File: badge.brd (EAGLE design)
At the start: 90.7 x 92.4 mm, 178 parts, among them CN4 MicroUSB, IC3 MEGA8-AI, Q1 BSS138, Q2 BSS138, T1 MMUN2133LT1G, U1 TPS61090RSAR, U2 MCP73871, U3 LIS3DHTR, U4 MIC5225-3.3, Y1 16.00MHz

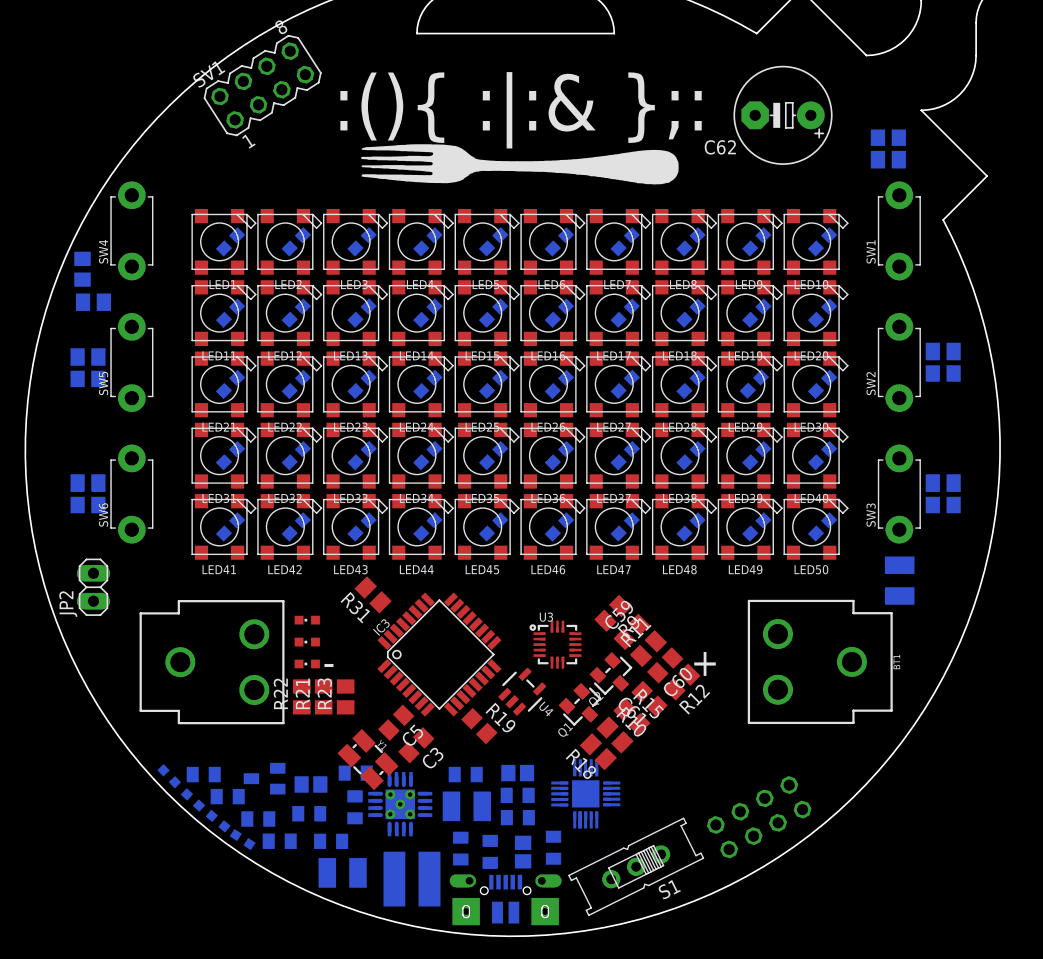
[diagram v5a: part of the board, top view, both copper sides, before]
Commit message: -wired all the pixels -cleaned up the schematic
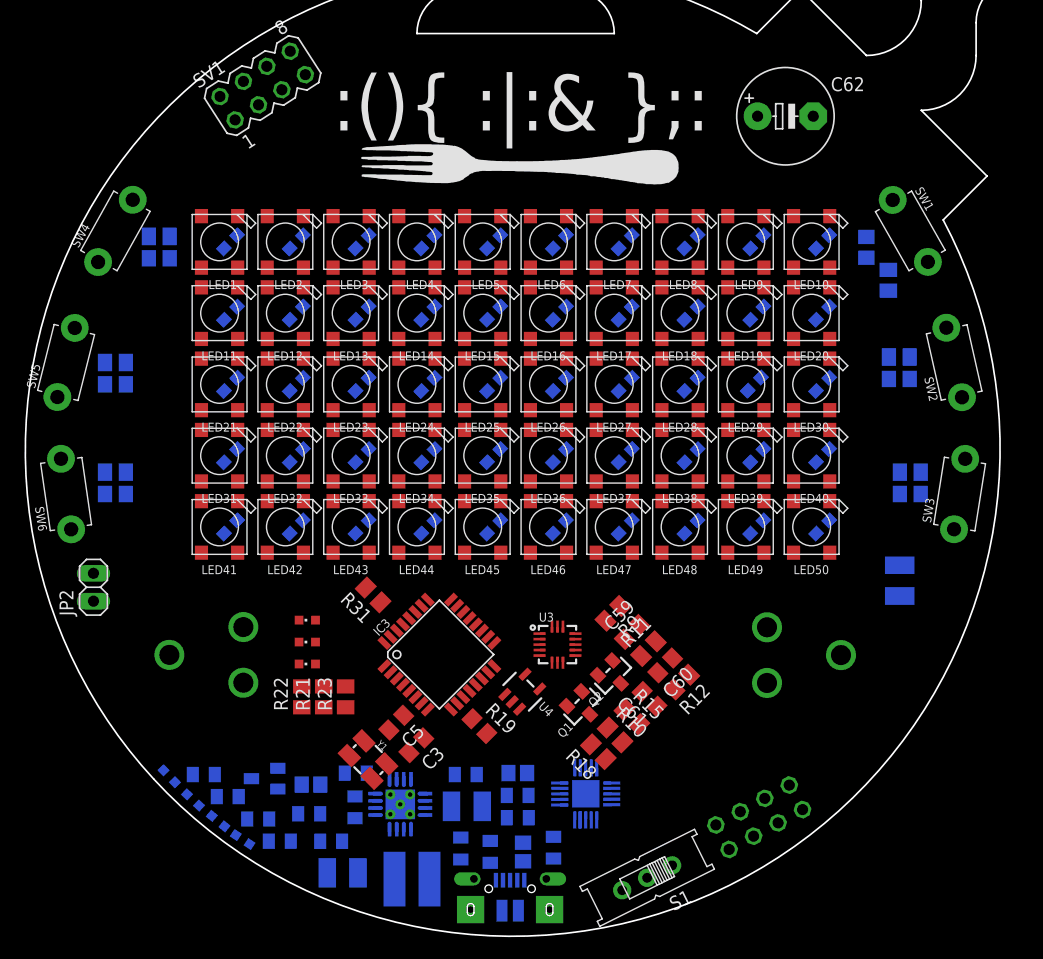
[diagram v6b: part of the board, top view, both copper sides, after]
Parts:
- moved R24 11.0 mm to (80.0, 60.5), turned to 270 degrees
- moved C63 10.2 mm to (78.0, 63.5), turned to 270 degrees
- moved R27 8.49 mm to (13.5, 64.5)
- moved C66 7.07 mm to (13.5, 62.5), turned to 0 degrees
- moved SW5 6.00 mm to (5.00, 53.0), turned to 75.9 degrees
- moved SW6 6.00 mm to (5.00, 41.0), turned to 98.2 degrees
- moved SW3 5.50 mm to (86.5, 41.0), turned to 81 degrees
- moved SW2 5.00 mm to (86.0, 53.0), turned to 102.7 degrees
- moved C64 4.03 mm to (81.0, 51.5)
- moved R25 4.03 mm to (81.0, 53.5)
- moved C65 3.16 mm to (82.0, 41.0)
- moved R26 3.16 mm to (82.0, 43.0)
- moved C68 2.69 mm to (9.50, 41.0)
- moved R29 2.69 mm to (9.50, 43.0)
- moved C67 2.55 mm to (9.50, 51.0)
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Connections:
- removed net N$18: C9.2, LED1.3-GND
- removed net VDD: LED10.1-VDD, LED11.1-VDD, LED12.1-VDD, LED13.1-VDD, LED14.1-VDD, LED15.1-VDD, LED16.1-VDD, LED17.1-VDD, LED18.1-VDD, LED19.1-VDD, LED2.1-VDD, LED20.1-VDD, LED21.1-VDD, LED22.1-VDD, LED23.1-VDD, LED24.1-VDD, LED25.1-VDD, LED26.1-VDD, LED27.1-VDD, LED28.1-VDD, LED29.1-VDD, LED3.1-VDD, LED30.1-VDD, LED31.1-VDD, LED32.1-VDD, LED33.1-VDD, LED34.1-VDD, LED35.1-VDD, LED36.1-VDD, LED37.1-VDD, LED38.1-VDD, LED39.1-VDD, LED4.1-VDD, LED40.1-VDD, LED41.1-VDD, LED42.1-VDD, LED43.1-VDD, LED44.1-VDD, LED45.1-VDD, LED46.1-VDD, LED47.1-VDD, LED48.1-VDD, LED49.1-VDD, LED5.1-VDD, LED50.1-VDD, LED6.1-VDD, LED7.1-VDD, LED8.1-VDD, LED9.1-VDD
- new net N$24: LED1.2-DOUT, LED2.4-DIN
- new net N$25: LED3.2-DOUT, LED4.4-DIN
- new net N$26: LED4.2-DOUT, LED5.4-DIN
- new net N$27: LED5.2-DOUT, LED6.4-DIN
- new net N$37: LED6.2-DOUT, LED7.4-DIN
- new net N$38: LED7.2-DOUT, LED8.4-DIN
- new net N$39: LED8.2-DOUT, LED9.4-DIN
- new net N$40: LED10.4-DIN, LED9.2-DOUT
- new net N$41: LED10.2-DOUT, LED11.4-DIN
- new net N$42: LED11.2-DOUT, LED12.4-DIN
- new net N$43: LED12.2-DOUT, LED13.4-DIN
- new net N$44: LED13.2-DOUT, LED14.4-DIN
- new net N$45: LED14.2-DOUT, LED15.4-DIN
- new net N$46: LED15.2-DOUT, LED16.4-DIN
- new net N$47: LED16.2-DOUT, LED17.4-DIN
- new net N$48: LED17.2-DOUT, LED18.4-DIN
- new net N$49: LED18.2-DOUT, LED19.4-DIN
- new net N$50: LED19.2-DOUT, LED20.4-DIN
- new net N$51: LED20.2-DOUT, LED21.4-DIN
- new net N$52: LED21.2-DOUT, LED22.4-DIN
- new net N$53: LED22.2-DOUT, LED23.4-DIN
- new net N$54: LED23.2-DOUT, LED24.4-DIN
- new net N$55: LED24.2-DOUT, LED25.4-DIN
- new net N$56: LED25.2-DOUT, LED26.4-DIN
- new net N$57: LED26.2-DOUT, LED27.4-DIN
- new net N$58: LED27.2-DOUT, LED28.4-DIN
- new net N$59: LED28.2-DOUT, LED29.4-DIN
- new net N$60: LED29.2-DOUT, LED30.4-DIN
- new net N$61: LED30.2-DOUT, LED31.4-DIN
- new net N$62: LED31.2-DOUT, LED32.4-DIN
- new net N$63: LED32.2-DOUT, LED33.4-DIN
- new net N$64: LED33.2-DOUT, LED34.4-DIN
- new net N$65: LED34.2-DOUT, LED35.4-DIN
- new net N$66: LED35.2-DOUT, LED36.4-DIN
- new net N$67: LED36.2-DOUT, LED37.4-DIN
- new net N$68: LED37.2-DOUT, LED38.4-DIN
- new net N$69: LED38.2-DOUT, LED39.4-DIN
- new net N$70: LED39.2-DOUT, LED40.4-DIN
- new net N$71: LED40.2-DOUT, LED41.4-DIN
- new net N$72: LED41.2-DOUT, LED42.4-DIN
- new net N$73: LED42.2-DOUT, LED43.4-DIN
- new net N$74: LED43.2-DOUT, LED44.4-DIN
- new net N$75: LED44.2-DOUT, LED45.4-DIN
- new net N$76: LED45.2-DOUT, LED46.4-DIN
- new net N$77: LED46.2-DOUT, LED47.4-DIN
- new net N$78: LED47.2-DOUT, LED48.4-DIN
- new net N$79: LED48.2-DOUT, LED49.4-DIN
- new net N$80: LED49.2-DOUT, LED50.4-DIN
- new net PIXEL_DATA: LED1.4-DIN, R19.2
- net +5V: now also C10.1, C11.1, C12.1, C13.1, C14.1, C15.1, C16.1, C17.1, C18.1, C19.1, C20.1, C21.1, C22.1, C23.1, C24.1, C25.1, C26.1, C27.1, C28.1, C29.1, C30.1, C31.1, C32.1, C33.1, C34.1, C35.1, C36.1, C37.1, C38.1, C39.1, C40.1, C41.1, C42.1, C43.1, C44.1, C45.1, C46.1, C47.1, C48.1, C49.1, C50.1, C51.1, C52.1, C53.1, C54.1, C55.1, C56.1, C57.1, C58.1, C9.1, LED1.1-VDD, LED10.1-VDD, LED11.1-VDD, LED12.1-VDD, LED13.1-VDD, LED14.1-VDD, LED15.1-VDD, LED16.1-VDD, LED17.1-VDD, LED18.1-VDD, LED19.1-VDD, LED2.1-VDD, LED20.1-VDD, LED21.1-VDD, LED22.1-VDD, LED23.1-VDD, LED24.1-VDD, LED25.1-VDD, LED26.1-VDD, LED27.1-VDD, LED28.1-VDD, LED29.1-VDD, LED3.1-VDD, LED30.1-VDD, LED31.1-VDD, LED32.1-VDD, LED33.1-VDD, LED34.1-VDD, LED35.1-VDD, LED36.1-VDD, LED37.1-VDD, LED38.1-VDD, LED39.1-VDD, LED4.1-VDD, LED40.1-VDD, LED41.1-VDD, LED42.1-VDD, LED43.1-VDD, LED44.1-VDD, LED45.1-VDD, LED46.1-VDD, LED47.1-VDD, LED48.1-VDD, LED49.1-VDD, LED5.1-VDD, LED50.1-VDD, LED6.1-VDD, LED7.1-VDD, LED8.1-VDD, LED9.1-VDD
- net GND: now also C10.2, C11.2, C12.2, C13.2, C14.2, C15.2, C16.2, C17.2, C18.2, C19.2, C20.2, C21.2, C22.2, C23.2, C24.2, C25.2, C26.2, C27.2, C28.2, C29.2, C30.2, C31.2, C32.2, C33.2, C34.2, C35.2, C36.2, C37.2, C38.2, C39.2, C40.2, C41.2, C42.2, C43.2, C44.2, C45.2, C46.2, C47.2, C48.2, C49.2, C50.2, C51.2, C52.2, C53.2, C54.2, C55.2, C56.2, C57.2, C58.2, C63.2, C64.2, C65.2, C66.2, C67.2, C68.2, C9.2, LED1.3-GND
- net N$17: now also LED2.2-DOUT, LED3.4-DIN; no longer C9.1, LED1.1-VDD

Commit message: haha forget to save fuck me
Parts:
- removed SV1: (no value), con-lstb:MA04-2
- added JP3: TCVR_HEADER, pinhead:2X04
- JP2: value (none) -> PIEZO_HEADER
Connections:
- removed net ADC1: U3.16
- removed net ADC2: U3.15
- removed net ADC3: U3.13
- removed net INT1: U3.11
- removed net STAT4: STAT2.A
- net 3.3V: now also JP3.7; no longer SV1.7
- net CE\: now also JP3.6; no longer SV1.6
- net CSN: now also JP3.5; no longer SV1.5
- net GND: now also JP3.8; no longer SV1.8
- net MISO: now also JP3.2; no longer SV1.2
- net MOSI: now also JP3.3; no longer SV1.3
- net SCK: now also JP3.4; no longer SV1.4
- net STAT2: now also STAT2.A
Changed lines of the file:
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@@
 <wire x1="55" y1="83" x2="51" y2="87" width="0.1524" layer="20" curve="90"/>
 <wire x1="51" y1="87" x2="41" y2="87" width="0.1524" layer="20"/>
+<dimension x1="0" y1="0" x2="100" y2="0" x3="50" y3="-6" textsize="1.778" layer="51"/>
+<dimension x1="100" y1="0" x2="100" y2="100" x3="105.5" y3="50" textsize="1.778" layer="51"/>
 </plain>
 <attributes>
@@
 <element name="U4" library="microbuilder" package="SOT23-5" value="MIC5225-3.3" x="46.6109125" y="22.974875" rot="R315"/>
 <element name="C61" library="resistor" library_urn="urn:adsk.eagle:library:348" package="C0805" package3d_urn="urn:adsk.eagle:package:26137/1" value="10µF" x="58.215828125" y="22.316" rot="R135"/>
-<element name="SV1" library="con-lstb" library_urn="urn:adsk.eagle:library:162" package="MA04-2" package3d_urn="urn:adsk.eagle:package:8368/1" value="" x="22.93" y="78.256" rot="R32.8">
-<attribute name="MF" value="" x="22.93" y="78.256" size="1.778" layer="27" rot="R32.8" display="off"/>
-<attribute name="MPN" value="" x="22.93" y="78.256" size="1.778" layer="27" rot="R32.8" display="off"/>
-<attribute name="OC_FARNELL" value="unknown" x="22.93" y="78.256" size="1.778" layer="27" rot="R32.8" display="off"/>
-<attribute name="OC_NEWARK" value="unknown" x="22.93" y="78.256" size="1.778" layer="27" rot="R32.8" display="off"/>
-</element>
 <element name="SW1" library="adafruit" library_urn="urn:adsk.eagle:library:420" package="TACT_PANA-EVQ" value="" x="82" y="65" rot="R299.6"/>
 <element name="SW2" library="adafruit" library_urn="urn:adsk.eagle:library:420" package="TACT_PANA-EVQ" value="" x="86" y="53" rot="R102.7"/>
@@
 <element name="R19" library="resistor" library_urn="urn:adsk.eagle:library:348" package="R0805" package3d_urn="urn:adsk.eagle:package:26059/1" value="470" x="42.697571875" y="19.832134375" rot="R315"/>
 <element name="C62" library="resistor" library_urn="urn:adsk.eagle:library:348" package="E5-8,5" package3d_urn="urn:adsk.eagle:package:25860/1" value="1F" x="70.61" y="75.46"/>
-<element name="JP2" library="pinhead" library_urn="urn:adsk.eagle:library:325" package="1X02" package3d_urn="urn:adsk.eagle:package:22435/2" value="" x="7.5" y="32.5" rot="R90"/>
+<element name="JP2" library="pinhead" library_urn="urn:adsk.eagle:library:325" package="1X02" package3d_urn="urn:adsk.eagle:package:22435/2" value="PIEZO_HEADER" x="7.5" y="32.5" rot="R90"/>
 <element name="S1" library="adafruit" library_urn="urn:adsk.eagle:library:420" package="EG1218" value="" x="58" y="6" rot="R206.5"/>
 <element name="STAT1" library="piboy_new" package="ADAFRUIT_CHIPLED_0603" value="GREEN" x="27" y="29.5" rot="R90"/>
@@
 <element name="R29" library="resistor" library_urn="urn:adsk.eagle:library:348" package="M0805" package3d_urn="urn:adsk.eagle:package:26079/1" value="1k" x="9.5" y="43" rot="MR180"/>
 <element name="C68" library="resistor" library_urn="urn:adsk.eagle:library:348" package="C0805" package3d_urn="urn:adsk.eagle:package:26137/1" value="100nF" x="9.5" y="41" rot="MR180"/>
+<element name="JP3" library="pinhead" library_urn="urn:adsk.eagle:library:325" package="2X04" package3d_urn="urn:adsk.eagle:package:22461/2" value="TCVR_HEADER" x="21" y="77" rot="R39.3"/>
 </elements>
 <signals>
@@
 <contactref element="R18" pad="1"/>
 <contactref element="C61" pad="2"/>
-<contactref element="SV1" pad="8"/>
 <contactref element="C62" pad="-"/>
 <contactref element="JP2" pad="2"/>
@@
 <contactref element="C67" pad="2"/>
 <contactref element="C68" pad="2"/>
+<contactref element="JP3" pad="8"/>
 <wire x1="74.65" y1="66.35" x2="73.15" y2="75.46" width="0" layer="19" extent="1-1"/>
 <wire x1="74.60104375" y1="64.601040625" x2="74.65" y2="66.35" width="0" layer="19" extent="1-16"/>
@@
 <wire x1="8.55" y1="51" x2="10.45" y2="41" width="0" layer="19" extent="16-16"/>
 <wire x1="4.20825" y1="49.847915625" x2="8.55" y2="51" width="0" layer="19" extent="16-16"/>
-<wire x1="25.4445875" y1="81.387425" x2="26.65" y2="66.35" width="0" layer="19" extent="1-1"/>
+<wire x1="23.143934375" y1="80.39595625" x2="20.65" y2="66.35" width="0" layer="19" extent="1-1"/>
 <wire x1="69.940290625" y1="11.01049375" x2="55.726865625" y2="4.86665625" width="0" layer="19" extent="1-1"/>
 </signal>
@@
 <contactref element="JP1" pad="1"/>
 <contactref element="IC3" pad="16"/>
-<contactref element="SV1" pad="2"/>
-<wire x1="44.06610625" y1="25.30510625" x2="19.03946875" y2="77.259609375" width="0" layer="19" extent="1-1"/>
+<contactref element="JP3" pad="2"/>
+<wire x1="44.06610625" y1="25.30510625" x2="17.247275" y2="75.56959375" width="0" layer="19" extent="1-1"/>
 <wire x1="64.263915625" y1="10.818721875" x2="44.06610625" y2="25.30510625" width="0" layer="19" extent="1-1"/>
 </signal>
@@
 <contactref element="JP1" pad="3"/>
 <contactref element="IC3" pad="17"/>
-<contactref element="SV1" pad="4"/>
-<wire x1="44.06610625" y1="27.415959375" x2="21.174509375" y2="78.63555" width="0" layer="19" extent="1-1"/>
+<contactref element="JP3" pad="4"/>
+<wire x1="44.06610625" y1="27.415959375" x2="19.212828125" y2="77.17838125" width="0" layer="19" extent="1-1"/>
 <wire x1="66.4961125" y1="12.030703125" x2="44.06610625" y2="27.415959375" width="0" layer="19" extent="1-1"/>
 </signal>
@@
 <contactref element="JP1" pad="4"/>
 <contactref element="IC3" pad="15"/>
-<contactref element="SV1" pad="3"/>
-<wire x1="43.50041875" y1="24.73941875" x2="22.550446875" y2="76.500509375" width="0" layer="19" extent="1-1"/>
+<contactref element="JP3" pad="3"/>
+<wire x1="43.50041875" y1="24.73941875" x2="20.821615625" y2="75.212828125" width="0" layer="19" extent="1-1"/>
 <wire x1="67.708096875" y1="9.798509375" x2="43.50041875" y2="24.73941875" width="0" layer="19" extent="1-1"/>
 </signal>
@@
 <contactref element="U4" pad="5"/>
 <contactref element="R9" pad="1"/>
-<contactref element="SV1" pad="7"/>
-<wire x1="48.47" y1="28.27" x2="26.820528125" y2="79.2523875" width="0" layer="19" extent="1-1"/>
+<contactref element="JP3" pad="7"/>
+<wire x1="48.47" y1="28.27" x2="24.752721875" y2="78.430403125" width="0" layer="19" extent="1-1"/>
 <wire x1="50.32" y1="28.62" x2="48.47" y2="28.27" width="0" layer="19" extent="1-1"/>
 <wire x1="46.85846875" y1="24.565934375" x2="48.47" y2="28.27" width="0" layer="19" extent="1-1"/>
@@
 <wire x1="36.298396875" y1="29.678703125" x2="55.59619375" y2="23.73223125" width="0" layer="19" extent="1-1"/>
 </signal>
-<signal name="INT1">
-<contactref element="U3" pad="11"/>
-</signal>
 <signal name="SDO">
 <contactref element="U3" pad="7"/>
@@
 <wire x1="52.874246875" y1="18.17375" x2="49.82" y2="25.92" width="0" layer="19" extent="1-1"/>
 </signal>
-<signal name="ADC1">
-<contactref element="U3" pad="16"/>
-</signal>
-<signal name="ADC2">
-<contactref element="U3" pad="15"/>
-</signal>
-<signal name="ADC3">
-<contactref element="U3" pad="13"/>
-</signal>
 <signal name="N$19">
 <contactref element="U3" pad="8"/>
 <contactref element="R9" pad="2"/>
 <wire x1="50.32" y1="25.92" x2="54.19718125" y2="29.449434375" width="0" layer="19" extent="1-1"/>
-</signal>
-<signal name="CE\">
-<contactref element="SV1" pad="6"/>
-</signal>
-<signal name="CSN">
-<contactref element="SV1" pad="5"/>
 </signal>
 <signal name="RX">
@@
 <signal name="STAT2">
 <contactref element="IC3" pad="1"/>
+<contactref element="STAT2" pad="A"/>
+<wire x1="27.75" y1="27.5" x2="34.035653125" y2="25.30510625" width="0" layer="19" extent="1-1"/>
 </signal>
 <signal name="STAT3">
@@
 <wire x1="27.75" y1="25.5" x2="34.601340625" y2="24.73941875" width="0" layer="19" extent="1-1"/>
 </signal>
-<signal name="STAT4">
-<contactref element="STAT2" pad="A"/>
-</signal>
 <signal name="N$20">
 <contactref element="STAT2" pad="C"/>
@@
 <wire x1="68.65" y1="35.65" x2="71.35" y2="40.35" width="0" layer="19" extent="1-1"/>
 </signal>
+<signal name="CSN">
+<contactref element="JP3" pad="5"/>
+</signal>
+<signal name="CE\">
+<contactref element="JP3" pad="6"/>
+</signal>
 </signals>
